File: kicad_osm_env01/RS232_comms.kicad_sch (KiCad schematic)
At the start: 16 parts, among them U19 MAX3223IPWR

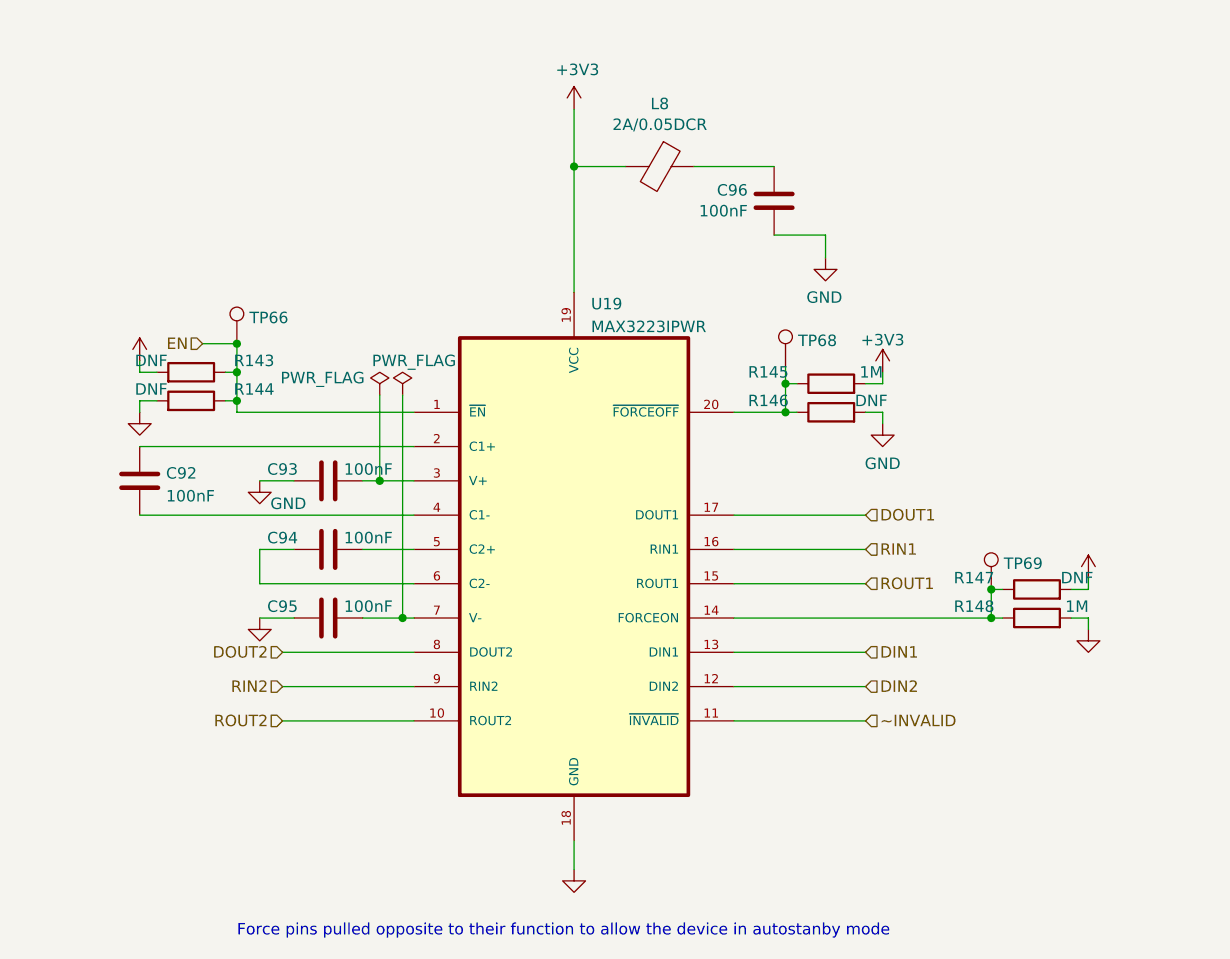
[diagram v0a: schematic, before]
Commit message: Schematics waiting review
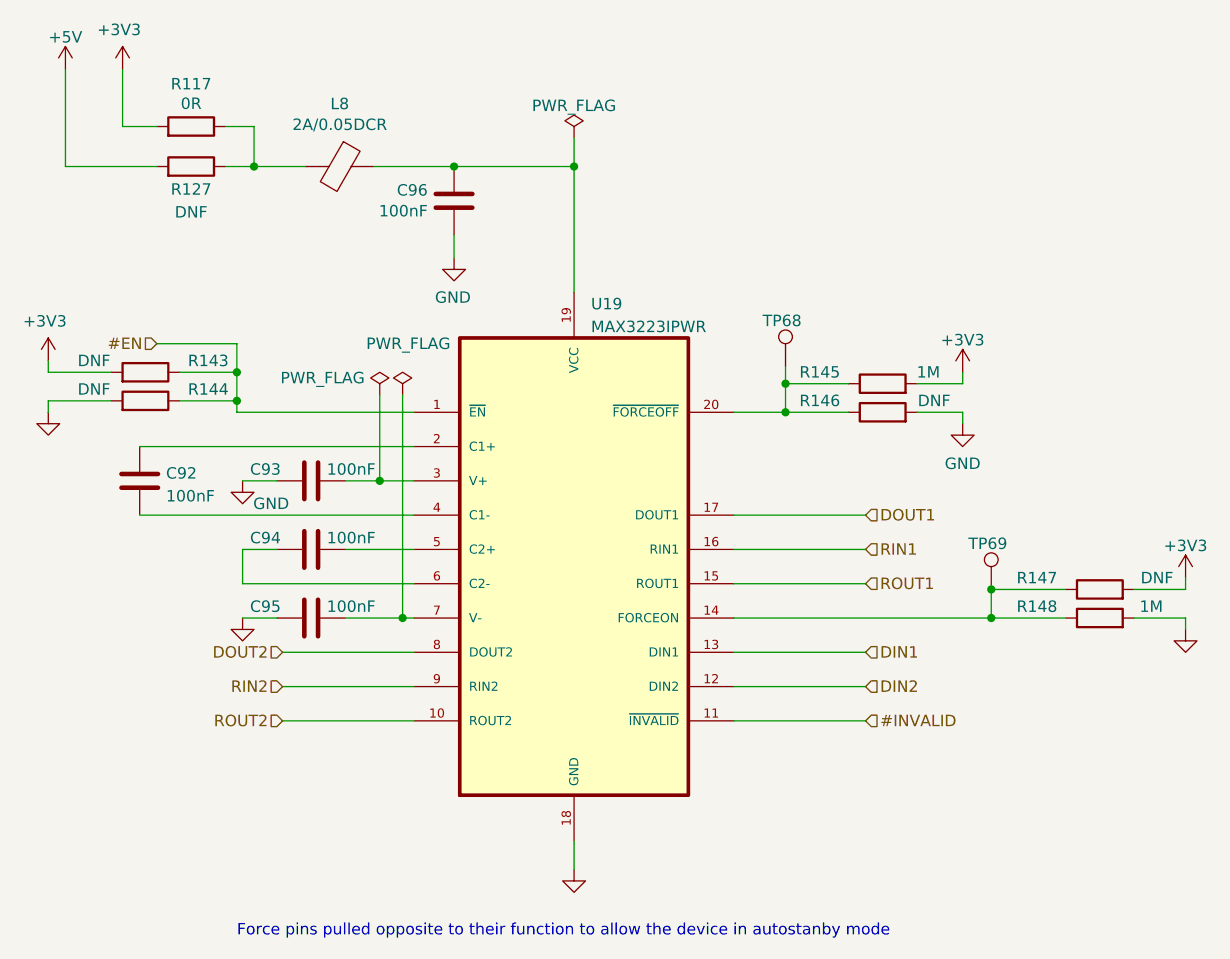
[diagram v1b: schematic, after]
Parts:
- removed TP66: ~, symbol Connector:TestPoint
- added R117: 0R, symbol device:R
- added R127: DNF, symbol device:R
- TP68: value TestPoint -> Test_Point
- TP69: value ~ -> Test_Point
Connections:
- net +3V3: now also R117.2; no longer L8.2, U19.19 (VCC)
- net at C96.1, L8.1: now also U19.19 (VCC)
- net EN renamed #EN
- net ~INVALID renamed #INVALID
- new net: L8.2, R117.1, R127.1
- new net +5V: R127.2
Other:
- company: (none) -> Devtank LTD
- title: (none) -> Open Smart Monitor
- moved on the sheet: C93, C94, C95, C96, L8, R143, R144, R145, R146, R147, R148

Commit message: before fixing devtank symbol issues
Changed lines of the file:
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@@
     (effects (font (size 1.27 1.27)) (justify left))
+  )
+  (symbol (lib_id "power:PWR_FLAG") (at 127.635 81.915 0) (unit 1)
+    (in_bom yes) (on_board yes)
+    (property "Reference" "#FLG03" (id 0) (at 127.635 80.01 0)
+      (effects (font (size 1.27 1.27)) hide)
+    )
+    (property "Value" "" (id 1) (at 121.285 80.01 0))
+    (property "Footprint" "" (id 2) (at 127.635 81.915 0)
+      (effects (font (size 1.27 1.27)) hide)
+    )
+    (property "Datasheet" "" (id 3) (at 127.635 81.915 0)
+      (effects (font (size 1.27 1.27)) hide)
+    )
+    (pin "1")
   )
   (symbol (lib_id "device:Ferrite_Bead") (at 123.19 56.515 270) (unit 1)
@@
       (effects (font (size 1.27 1.27)) hide)
     )
-    (property "Value" "+3V3" (id 1) (at 98.679 41.3258 0))
+    (property "Value" "" (id 1) (at 98.679 41.3258 0))
     (property "Footprint" "" (id 2) (at 99.06 45.72 0)
       (effects (font (size 1.27 1.27)) hide)
@@
       (effects (font (size 1.27 1.27)) hide)
     )
-    (property "Value" "+3V3" (id 1) (at 192.405 75.7992 0))
+    (property "Value" "" (id 1) (at 192.405 75.7992 0))
     (property "Footprint" "" (id 2) (at 192.405 79.375 0)
       (effects (font (size 1.27 1.27)) hide)
@@
       (effects (font (size 1.27 1.27)) hide)
     )
-    (property "Value" "+3V3" (id 1) (at 90.424 73.7108 0))
+    (property "Value" "" (id 1) (at 90.424 73.7108 0))
     (property "Footprint" "" (id 2) (at 90.805 78.105 0)
       (effects (font (size 1.27 1.27)) hide)
@@
     (pin "1")
   )
-  (symbol (lib_id "power:PWR_FLAG") (at 127.635 81.915 0) (unit 1)
-    (in_bom yes) (on_board yes)
-    (property "Reference" "#FLG03" (id 0) (at 127.635 80.01 0)
-      (effects (font (size 1.27 1.27)) hide)
-    )
-    (property "Value" "PWR_FLAG" (id 1) (at 121.285 80.01 0))
-    (property "Footprint" "" (id 2) (at 127.635 81.915 0)
-      (effects (font (size 1.27 1.27)) hide)
-    )
-    (property "Datasheet" "~" (id 3) (at 127.635 81.915 0)
-      (effects (font (size 1.27 1.27)) hide)
-    )
-    (pin "1")
-  )
   (symbol (lib_id "Device:C") (at 120.015 99.06 90) (unit 1)
     (in_bom yes) (on_board yes)
@@
     (pin "2")
   )
-  (symbol (lib_name "PWR_FLAG_1") (lib_id "power:PWR_FLAG") (at 149.225 53.34 0) (unit 1)
+  (symbol (lib_id "power:PWR_FLAG") (at 149.225 53.34 0) (unit 1)
     (in_bom yes) (on_board yes) (fields_autoplaced)
     (property "Reference" "#FLG0106" (id 0) (at 149.225 51.435 0)
       (effects (font (size 1.27 1.27)) hide)
     )
-    (property "Value" "PWR_FLAG" (id 1) (at 149.225 49.7642 0))
+    (property "Value" "" (id 1) (at 149.225 49.7642 0))
     (property "Footprint" "" (id 2) (at 149.225 53.34 0)
       (effects (font (size 1.27 1.27)) hide)
@@
     (pin "2")
   )
+  (symbol (lib_id "power:PWR_FLAG") (at 130.175 81.915 0) (unit 1)
+    (in_bom yes) (on_board yes)
+    (property "Reference" "#FLG06" (id 0) (at 130.175 80.01 0)
+      (effects (font (size 1.27 1.27)) hide)
+    )
+    (property "Value" "" (id 1) (at 130.81 77.47 0))
+    (property "Footprint" "" (id 2) (at 130.175 81.915 0)
+      (effects (font (size 1.27 1.27)) hide)
+    )
+    (property "Datasheet" "" (id 3) (at 130.175 81.915 0)
+      (effects (font (size 1.27 1.27)) hide)
+    )
+    (pin "1")
+  )
   (symbol (lib_id "OSM_env01:GND") (at 192.405 85.09 0) (unit 1)
     (in_bom yes) (on_board yes) (fields_autoplaced)
@@
     (pin "1")
   )
-  (symbol (lib_id "power:PWR_FLAG") (at 130.175 81.915 0) (unit 1)
-    (in_bom yes) (on_board yes)
-    (property "Reference" "#FLG06" (id 0) (at 130.175 80.01 0)
-      (effects (font (size 1.27 1.27)) hide)
-    )
-    (property "Value" "PWR_FLAG" (id 1) (at 130.81 76.2 0))
-    (property "Footprint" "" (id 2) (at 130.175 81.915 0)
-      (effects (font (size 1.27 1.27)) hide)
-    )
-    (property "Datasheet" "~" (id 3) (at 130.175 81.915 0)
-      (effects (font (size 1.27 1.27)) hide)
-    )
-    (pin "1")
-  )
   (symbol (lib_id "power:+3V3") (at 217.17 102.235 0) (unit 1)
     (in_bom yes) (on_board yes) (fields_autoplaced)
@@
       (effects (font (size 1.27 1.27)) hide)
     )
-    (property "Value" "+3V3" (id 1) (at 217.17 98.6592 0))
+    (property "Value" "" (id 1) (at 217.17 98.6592 0))
     (property "Footprint" "" (id 2) (at 217.17 102.235 0)
       (effects (font (size 1.27 1.27)) hide)

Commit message: started layout with throwdown
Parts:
- C92, C93, C94, C95: value 100nF -> (none)
- C96: value 100nF -> (none); footprint Capacitor_SMD:C_0603_1608Metric -> (none); symbol device:C -> Device:C
- L8: value 2A/0.05DCR -> (none); footprint Inductor_SMD:L_0402_1005Metric -> (none); symbol device:Ferrite_Bead -> Device:FerriteBead
- R117: value 0R -> (none); symbol device:R -> Device:R
- R127: value DNF -> (none); symbol device:R -> Device:R
- R143, R144, R146, R147: value DNF -> (none)
- R145, R148: value 1M -> (none)
- TP68, TP69: value Test_Point -> (none)
- U19: value MAX3223IPWR -> (none); footprint SOP65P640X120-20N -> (none)
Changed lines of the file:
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@@
       (effects (font (size 1.27 1.27)) hide)
     )
-    (property "Value" "" (id 1) (at 121.285 80.01 0))
+    (property "Value" "PWR_FLAG" (id 1) (at 121.285 80.01 0))
     (property "Footprint" "" (id 2) (at 127.635 81.915 0)
       (effects (font (size 1.27 1.27)) hide)
@@
     (pin "1")
   )
-  (symbol (lib_id "device:Ferrite_Bead") (at 123.19 56.515 270) (unit 1)
+  (symbol (lib_id "Device:FerriteBead") (at 123.19 56.515 270) (unit 1)
     (in_bom yes) (on_board yes)
     (property "Reference" "L8" (id 0) (at 123.19 49.5554 90))
-    (property "Value" "2A/0.05DCR" (id 1) (at 123.19 51.8668 90))
-    (property "Footprint" "Inductor_SMD:L_0402_1005Metric" (id 2) (at 123.19 54.737 90)
+    (property "Value" "" (id 1) (at 123.19 51.8668 90))
+    (property "Footprint" "" (id 2) (at 123.19 54.737 90)
       (effects (font (size 1.27 1.27)) hide)
     )
@@
     (pin "2")
   )
-  (symbol (lib_id "device:R") (at 106.68 52.07 270) (mirror x) (unit 1)
+  (symbol (lib_id "Device:R") (at 106.68 52.07 270) (mirror x) (unit 1)
     (in_bom yes) (on_board yes)
     (property "Reference" "R117" (id 0) (at 106.68 47.3542 90))
-    (property "Value" "0R" (id 1) (at 106.68 49.53 90))
+    (property "Value" "" (id 1) (at 106.68 49.53 90))
     (property "Footprint" "" (id 2) (at 106.68 53.848 90)
       (effects (font (size 1.27 1.27)) hide)
@@
     (pin "2")
   )
-  (symbol (lib_id "device:C") (at 135.89 60.325 0) (mirror y) (unit 1)
+  (symbol (lib_id "Device:C") (at 135.89 60.325 0) (mirror y) (unit 1)
     (in_bom yes) (on_board yes)
     (property "Reference" "C96" (id 0) (at 132.969 59.1566 0)
       (effects (font (size 1.27 1.27)) (justify left))
     )
-    (property "Value" "100nF" (id 1) (at 132.969 61.468 0)
-      (effects (font (size 1.27 1.27)) (justify left))
-    )
-    (property "Footprint" "Capacitor_SMD:C_0603_1608Metric" (id 2) (at 134.9248 64.135 0)
+    (property "Value" "" (id 1) (at 132.969 61.468 0)
+      (effects (font (size 1.27 1.27)) (justify left))
+    )
+    (property "Footprint" "" (id 2) (at 134.9248 64.135 0)
       (effects (font (size 1.27 1.27)) hide)
     )
@@
       (effects (font (size 1.27 1.27)) (justify left))
     )
-    (property "Value" "MAX3223IPWR" (id 1) (at 151.1047 74.3259 0)
-      (effects (font (size 1.27 1.27)) (justify left))
-    )
-    (property "Footprint" "SOP65P640X120-20N" (id 2) (at 149.225 100.965 0)
+    (property "Value" "" (id 1) (at 151.1047 74.3259 0)
+      (effects (font (size 1.27 1.27)) (justify left))
+    )
+    (property "Footprint" "" (id 2) (at 149.225 100.965 0)
       (effects (font (size 1.27 1.27)) (justify left bottom) hide)
     )
@@
     (in_bom yes) (on_board yes)
     (property "Reference" "R144" (id 0) (at 108.585 81.28 90))
-    (property "Value" "DNF" (id 1) (at 95.885 81.28 90))
+    (property "Value" "" (id 1) (at 95.885 81.28 90))
     (property "Footprint" "" (id 2) (at 101.6 84.328 90)
       (effects (font (size 1.27 1.27)) hide)
@@
       (effects (font (size 1.27 1.27)) (justify left))
     )
-    (property "Value" "100nF" (id 1) (at 103.886 93.1422 0)
+    (property "Value" "" (id 1) (at 103.886 93.1422 0)
       (effects (font (size 1.27 1.27)) (justify left))
     )
@@
       (effects (font (size 1.27 1.27)) (justify left))
     )
-    (property "Value" "Test_Point" (id 1) (at 174.117 77.1402 0)
+    (property "Value" "" (id 1) (at 174.117 77.1402 0)
       (effects (font (size 1.27 1.27)) (justify left) hide)
     )
@@
       (effects (font (size 1.27 1.27)) hide)
     )
-    (property "Value" "" (id 1) (at 98.679 41.3258 0))
+    (property "Value" "+3V3" (id 1) (at 98.679 41.3258 0))
     (property "Footprint" "" (id 2) (at 99.06 45.72 0)
       (effects (font (size 1.27 1.27)) hide)
@@
       (effects (font (size 1.27 1.27)) hide)
     )
-    (property "Value" "" (id 1) (at 192.405 75.7992 0))
+    (property "Value" "+3V3" (id 1) (at 192.405 75.7992 0))
     (property "Footprint" "" (id 2) (at 192.405 79.375 0)
       (effects (font (size 1.27 1.27)) hide)
@@
       (effects (font (size 1.27 1.27)) hide)
     )
-    (property "Value" "" (id 1) (at 90.424 73.7108 0))
+    (property "Value" "+3V3" (id 1) (at 90.424 73.7108 0))
     (property "Footprint" "" (id 2) (at 90.805 78.105 0)
       (effects (font (size 1.27 1.27)) hide)
@@
     (pin "1")
   )
-  (symbol (lib_id "OSM_env01:GND") (at 112.395 91.44 0) (unit 1)
+  (symbol (lib_id "power:GND") (at 112.395 91.44 0) (unit 1)
     (in_bom yes) (on_board yes)
     (property "Reference" "#PWR0169" (id 0) (at 112.395 97.79 0)
@@
     (pin "1")
   )
-  (symbol (lib_id "device:R") (at 106.68 56.515 270) (mirror x) (unit 1)
+  (symbol (lib_id "Device:R") (at 106.68 56.515 270) (mirror x) (unit 1)
     (in_bom yes) (on_board yes)
     (property "Reference" "R127" (id 0) (at 106.68 59.055 90))
-    (property "Value" "DNF" (id 1) (at 106.68 61.595 90))
+    (property "Value" "" (id 1) (at 106.68 61.595 90))
     (property "Footprint" "" (id 2) (at 106.68 58.293 90)
       (effects (font (size 1.27 1.27)) hide)
@@
     (in_bom yes) (on_board yes)
     (property "Reference" "R145" (id 0) (at 176.53 79.375 90))
-    (property "Value" "1M" (id 1) (at 188.595 79.375 90))
+    (property "Value" "" (id 1) (at 188.595 79.375 90))
     (property "Footprint" "" (id 2) (at 183.515 82.423 90)
       (effects (font (size 1.27 1.27)) hide)
@@
     (in_bom yes) (on_board yes)
     (property "Reference" "R147" (id 0) (at 200.66 102.235 90))
-    (property "Value" "DNF" (id 1) (at 213.995 102.235 90))
+    (property "Value" "" (id 1) (at 213.995 102.235 90))
     (property "Footprint" "" (id 2) (at 207.645 105.283 90)
       (effects (font (size 1.27 1.27)) hide)
@@
     (in_bom yes) (on_board yes)
     (property "Reference" "C93" (id 0) (at 114.935 90.17 90))
-    (property "Value" "100nF" (id 1) (at 124.46 90.17 90))
+    (property "Value" "" (id 1) (at 124.46 90.17 90))
     (property "Footprint" "" (id 2) (at 123.825 90.4748 0)
       (effects (font (size 1.27 1.27)) hide)
@@
     (in_bom yes) (on_board yes)
     (property "Reference" "C94" (id 0) (at 114.935 97.79 90))
-    (property "Value" "100nF" (id 1) (at 124.46 97.79 90))
+    (property "Value" "" (id 1) (at 124.46 97.79 90))
     (property "Footprint" "" (id 2) (at 123.825 98.0948 0)
       (effects (font (size 1.27 1.27)) hide)
@@
       (effects (font (size 1.27 1.27)) hide)
     )
-    (property "Value" "" (id 1) (at 149.225 49.7642 0))
+    (property "Value" "PWR_FLAG" (id 1) (at 149.225 49.7642 0))
     (property "Footprint" "" (id 2) (at 149.225 53.34 0)
       (effects (font (size 1.27 1.27)) hide)
@@
     (in_bom yes) (on_board yes)
     (property "Reference" "C95" (id 0) (at 114.935 105.41 90))
-    (property "Value" "100nF" (id 1) (at 124.46 105.41 90))
+    (property "Value" "" (id 1) (at 124.46 105.41 90))
     (property "Footprint" "" (id 2) (at 123.825 105.7148 0)
       (effects (font (size 1.27 1.27)) hide)
@@
       (effects (font (size 1.27 1.27)) hide)
     )
-    (property "Value" "" (id 1) (at 130.81 77.47 0))
+    (property "Value" "PWR_FLAG" (id 1) (at 130.81 77.47 0))
     (property "Footprint" "" (id 2) (at 130.175 81.915 0)
       (effects (font (size 1.27 1.27)) hide)
@@
     (pin "1")
   )
-  (symbol (lib_id "OSM_env01:GND") (at 192.405 85.09 0) (unit 1)
+  (symbol (lib_id "power:GND") (at 192.405 85.09 0) (unit 1)
     (in_bom yes) (on_board yes) (fields_autoplaced)
     (property "Reference" "#PWR0175" (id 0) (at 192.405 91.44 0)
@@
     (in_bom yes) (on_board yes)
     (property "Reference" "R148" (id 0) (at 200.66 105.41 90))
-    (property "Value" "1M" (id 1) (at 213.36 105.41 90))
+    (property "Value" "" (id 1) (at 213.36 105.41 90))
     (property "Footprint" "" (id 2) (at 207.645 108.458 90)
       (effects (font (size 1.27 1.27)) hide)
@@
     (in_bom yes) (on_board yes)
     (property "Reference" "R143" (id 0) (at 108.585 78.105 90))
-    (property "Value" "DNF" (id 1) (at 95.885 78.105 90))
+    (property "Value" "" (id 1) (at 95.885 78.105 90))
     (property "Footprint" "" (id 2) (at 101.6 81.153 90)
       (effects (font (size 1.27 1.27)) hide)
@@
     (in_bom yes) (on_board yes)
     (property "Reference" "R146" (id 0) (at 176.53 82.55 90))
-    (property "Value" "DNF" (id 1) (at 189.23 82.55 90))
+    (property "Value" "" (id 1) (at 189.23 82.55 90))
     (property "Footprint" "" (id 2) (at 183.515 85.598 90)
       (effects (font (size 1.27 1.27)) hide)
@@
     (pin "2")
   )
-  (symbol (lib_id "OSM_env01:GND") (at 135.89 66.675 0) (mirror y) (unit 1)
+  (symbol (lib_id "power:GND") (at 135.89 66.675 0) (mirror y) (unit 1)
     (in_bom yes) (on_board yes)
     (property "Reference" "#PWR0173" (id 0) (at 135.89 73.025 0)
@@
       (effects (font (size 1.27 1.27)) (justify left))
     )
-    (property "Value" "Test_Point" (id 1) (at 196.977 101.9052 0)
+    (property "Value" "" (id 1) (at 196.977 101.9052 0)
       (effects (font (size 1.27 1.27)) (justify left) hide)
     )
@@
       (effects (font (size 1.27 1.27)) hide)
     )
-    (property "Value" "" (id 1) (at 217.17 98.6592 0))
+    (property "Value" "+3V3" (id 1) (at 217.17 98.6592 0))
     (property "Footprint" "" (id 2) (at 217.17 102.235 0)
       (effects (font (size 1.27 1.27)) hide)
